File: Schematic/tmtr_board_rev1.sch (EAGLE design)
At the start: 25 parts, among them IC1 MEGA8-AI, J1 POWER_JACKPTH_LOCK

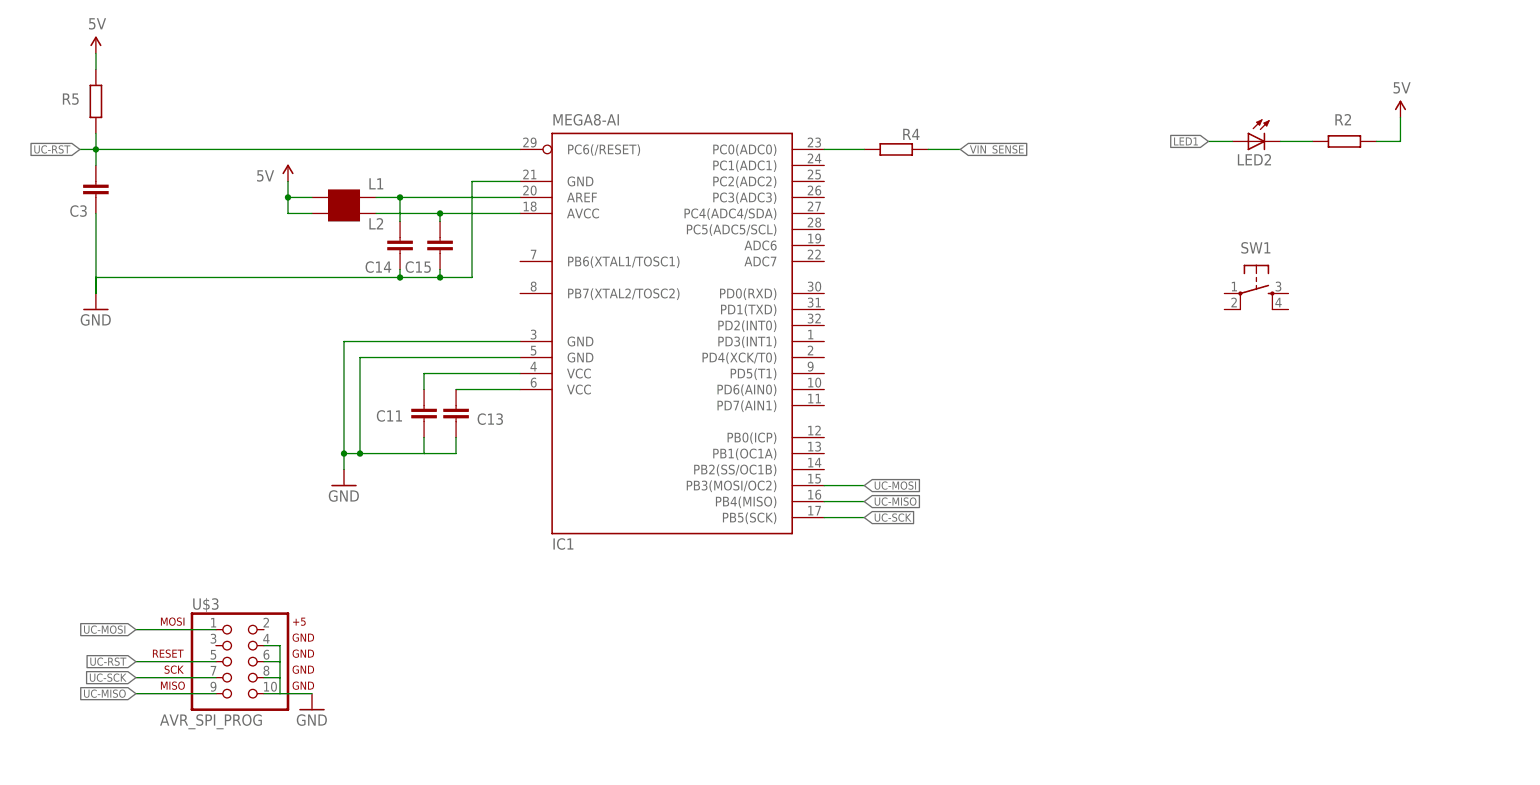
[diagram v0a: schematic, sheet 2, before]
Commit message: 
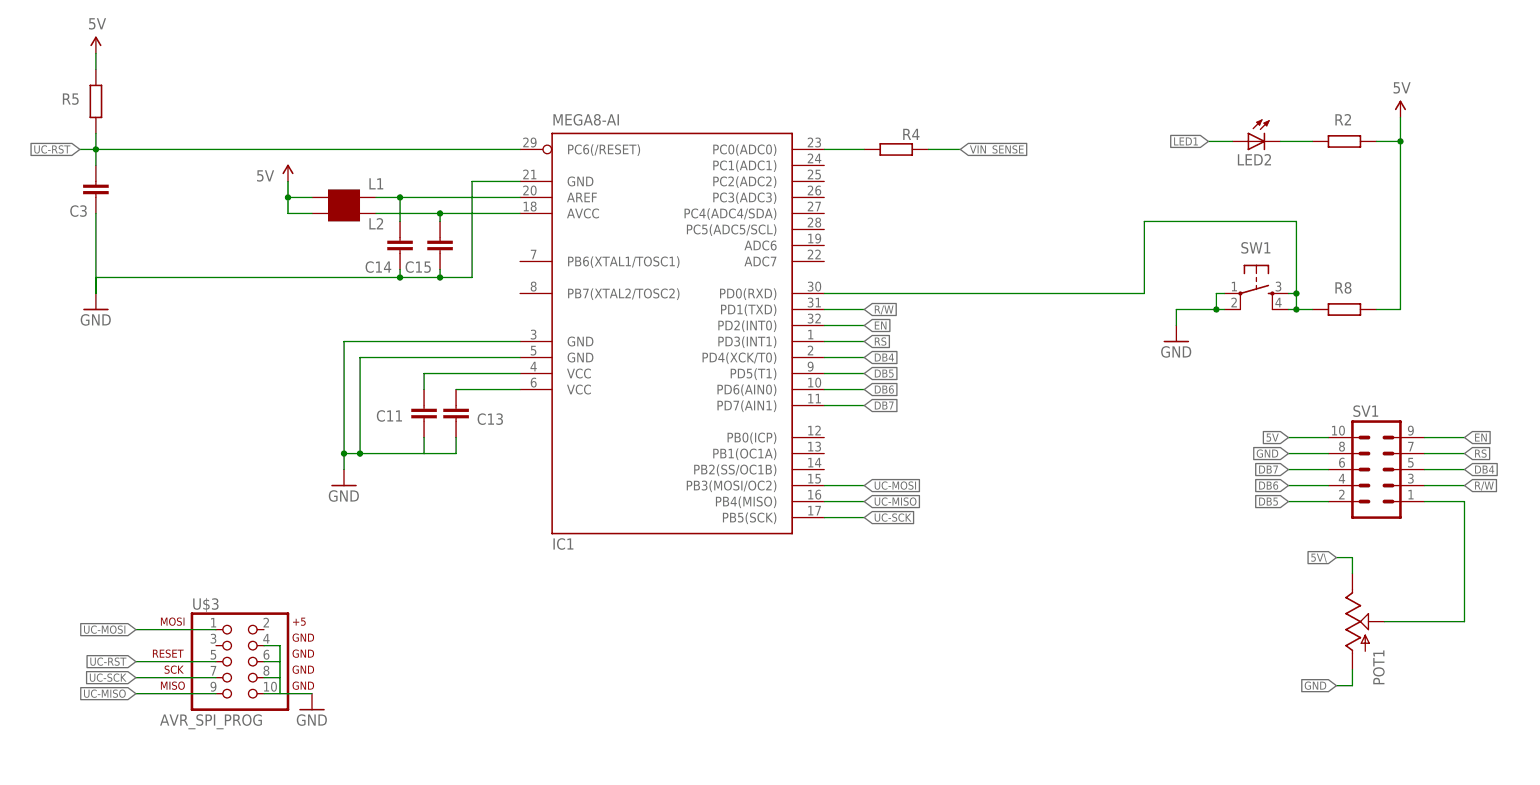
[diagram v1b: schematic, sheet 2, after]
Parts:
- added C12: (no value), rcl:CPOL-EUE2.5-6
- added C6: (no value), SparkFun1:CAPPTH
- added POT1: POT100K_3362U, SparkFun5:POT100K_3362U
- added R6, R7: (no value), resistor:R-EU_0204/5
- added R8: (no value), resistor:R-EU_M0805
- added SV1: (no value), con-lstb:MA05-2
- added U6: V_REG_317SINK, SparkFun4:V_REG_317SINK
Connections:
- new net 3.3V: R7.1, U6.OUT
- new net 5V\: POT1.E
- new net DB4: IC1.PD4(XCK/T0)
- new net DB5: IC1.PD5(T1), SV1.2
- new net DB6: IC1.PD6(AIN0), SV1.4
- new net DB7: IC1.PD7(AIN1), SV1.6
- new net EN: IC1.PD2(INT0)
- new net N$13: POT1.S, SV1.1
- new net N$20: R6.2, R7.2, U6.ADJ
- new net N$21: C12.+, C6.2
- new net N$9: IC1.PD0(RXD), R8.2, SW1.3, SW1.4
- new net R/W: IC1.PD1(TXD)
- new net RS: IC1.PD3(INT1)
- net 5V: now also R8.1, SV1.10, U6.IN
- net GND: now also C12.-, C6.1, POT1.A, R6.1, SV1.8, SW1.1, SW1.2

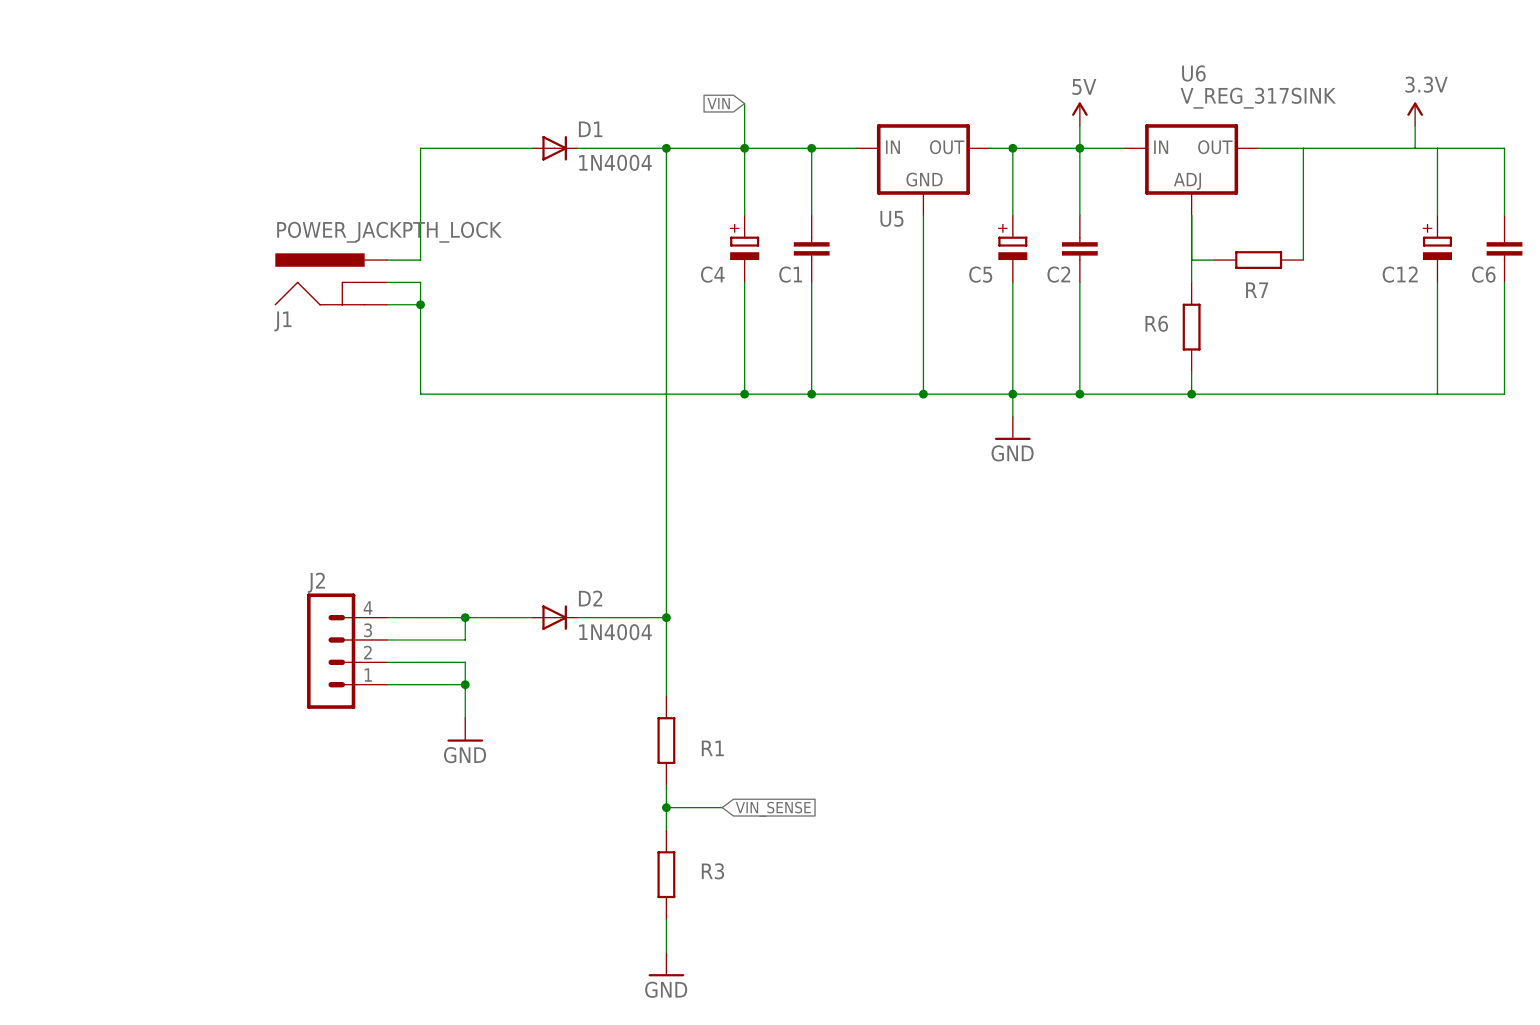
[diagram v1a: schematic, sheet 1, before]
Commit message: 
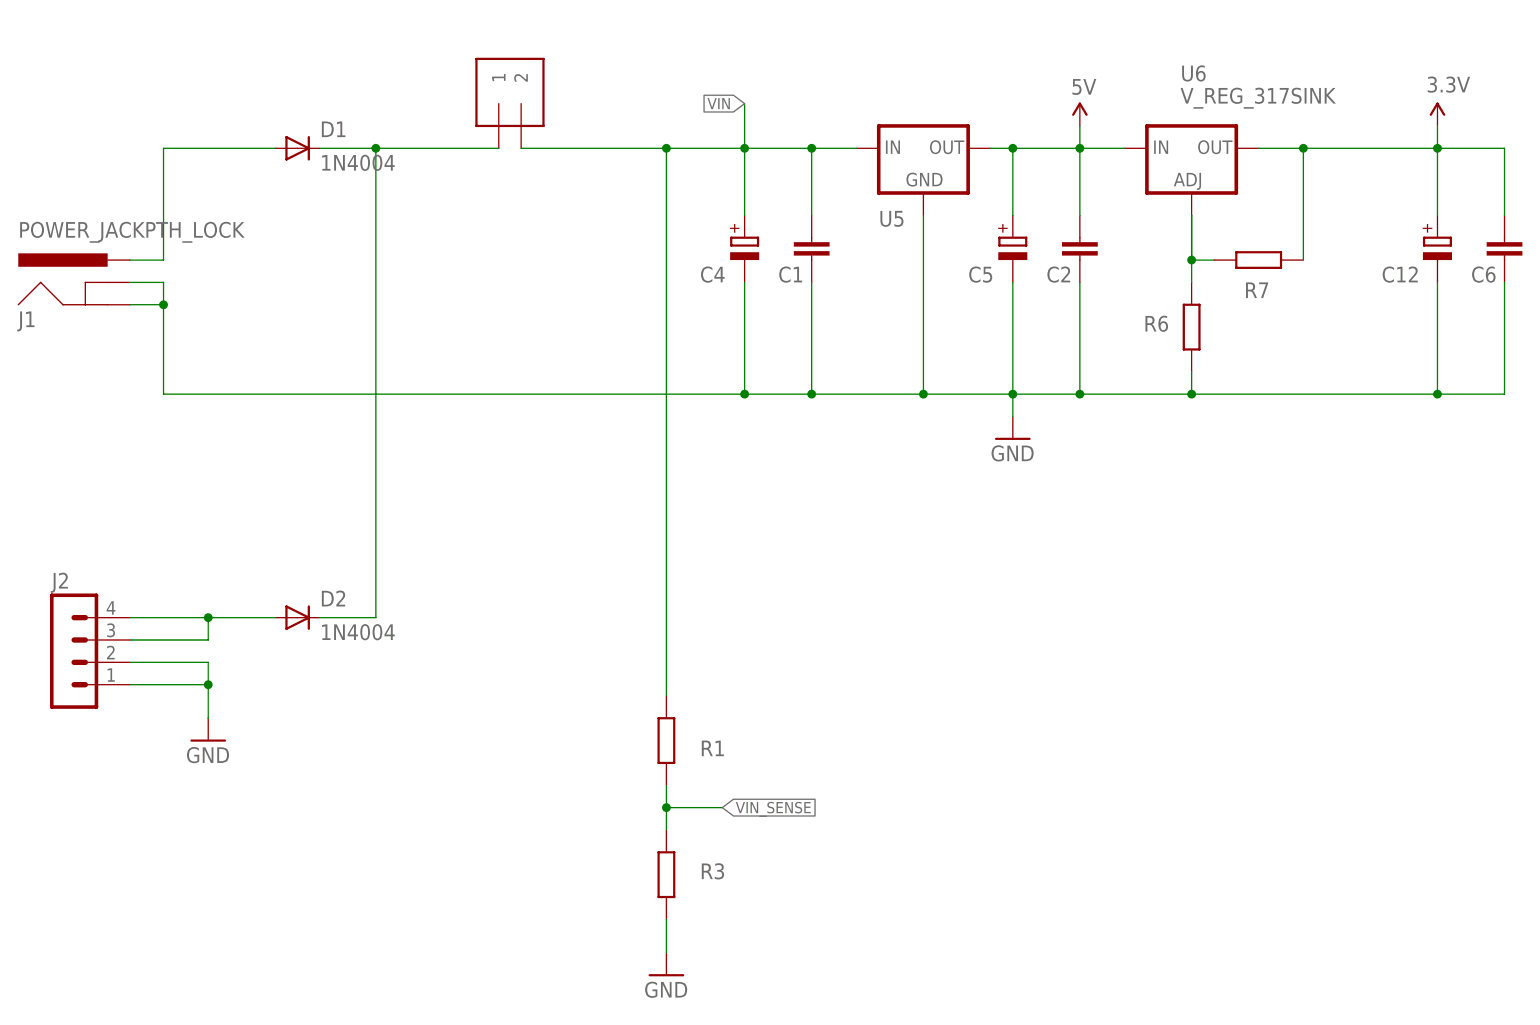
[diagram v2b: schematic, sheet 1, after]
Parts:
- added C7, C8: (no value), SparkFun1:CAP0805
- added IC2, IC3: MAX31855, adafruit:MAX6675
- added J3, J4, J5: 1X2-3.5MM, adafruit:1X2-3.5MM
- added LED1: (no value), led:LEDCHIPLED_0805
- added R9: (no value), resistor:R-EU_M0805
- renumbered SW1 to AVG_SW
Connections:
- removed net 5V\: POT1.E
- removed net N$21: C12.+, C6.2
- removed net N$8: C13.2, IC1.VCC@2
- new net CS_TS_IC0: IC1.PC4(ADC4/SDA), IC2./CS
- new net CS_TS_IC1: IC1.PB1(OC1A), IC3./CS
- new net DO_TS_IC0: IC1.PC3(ADC3), IC2.DO
- new net DO_TS_IC1: IC1.PB0(ICP), IC3.DO
- new net LED2: IC1.PC2(ADC2), LED2.A
- new net N$10: LED1.C, R9.2
- new net SCK_TS_IC0: IC1.PC5(ADC5/SCL), IC2.SCK
- new net SCK_TS_IC1: IC1.PB2(SS/OC1B), IC3.SCK
- new net T+0: IC2.T+, J3.1
- new net T+1: IC3.T+, J4.1
- new net T-0: IC2.T-, J3.2
- new net T-1: IC3.T-, J4.2
- net 3.3V: now also C12.+, C6.2, C7.1, C8.1, IC2.VCC, IC3.VCC
- net 5V: now also C11.2, C13.2, IC1.VCC@1, IC1.VCC@2, POT1.E, R9.1
- net GND: now also C7.2, C8.2, IC2.GND, IC3.GND
- net LED1: now also IC1.PC1(ADC1), LED1.A; no longer LED2.A
- net N$4: now also D1.C, D2.C, J5.1; no longer C11.2, IC1.VCC@1
- net VIN: now also J5.2; no longer D1.C, D2.C
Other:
- moved on the sheet: D1, D2, J1, J2

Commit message: 
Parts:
- removed AVG_SW: (no value), SparkFun1:TAC_SWITCHPTH
- removed C14: (no value), SparkFun1:CAP0805
- removed IC3: MAX31855, adafruit:MAX6675
- removed LED1, LED2: (no value), led:LEDCHIPLED_0805
- removed POT1: POT100K_3362U, SparkFun5:POT100K_3362U
- removed SV1: (no value), con-lstb:MA05-2
- removed U6: V_REG_317SINK, SparkFun4:V_REG_317SINK
- added C10: (no value), SparkFun1:CAP0805
- added J7, J8: 22-23-2021, con-molex:22-23-2021
- added LED3, LED4: (no value), led:LEDCHIPLED_0805
- added R10, R11: (no value), resistor:R-EU_M0805
- added U1: (no value), v-reg:78XXS
- added U2: LD117AS12TR, v-reg:LD117AS12TR
- C1: device SparkFun1:CAPPTH -> rcl:CPOL-EUE5-6
- C12: device rcl:CPOL-EUE2.5-6 -> SparkFun1:CAP0805
- C3: device SparkFun1:CAP0805 -> rcl:CPOL-EUE2.5-6
- C4: device rcl:CPOL-EUE5-6 -> SparkFun1:CAPPTH
- D1, D2: value 1N4004 -> (none); device diode:1N4004 -> semicon-smd-ipc:D-FILL-SMB
- J1: value POWER_JACKPTH_LOCK -> 22-23-2021; device SparkFun4:POWER_JACKPTH_LOCK -> con-molex:22-23-2021
- J2: value (none) -> POWER_JACKPTH_LOCK; device con-lstb:MA04-1 -> SparkFun4:POWER_JACKPTH_LOCK
- J3: value 1X2-3.5MM -> (none); device adafruit:1X2-3.5MM -> con-lstb:MA04-1
- J4: value 1X2-3.5MM -> 22-23-2021; device adafruit:1X2-3.5MM -> con-molex:22-23-2021
- J5: value 1X2-3.5MM -> (none); device adafruit:1X2-3.5MM -> con-lstb:MA05-2
- R6, R7: device resistor:R-EU_0204/5 -> resistor:R-EU_M0805
- U5: value (none) -> MAX31855; device v-reg:78XXS -> adafruit:MAX6675
- renumbered C15 to C9, IC1 to U3, IC2 to U4, U$3 to J6
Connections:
- net 3.3V: now also C12.1, C13.1, C5.+, R1.2, U2.OUT, U5.VCC; no longer C12.+, C7.1, C8.1, IC3.VCC, R7.1, U6.OUT
- net 5V: now also C10.2, C3.+, C4.2, J5.10, R10.1, R6.1, U1.OUT, U2.IN; no longer C13.2, C2.2, C5.+, POT1.E, R2.1, SV1.10, U5.OUT, U6.IN
- net CS_TS_IC1: now also U5./CS; no longer IC3./CS
- net DB4: now also J5.5
- net DB5: now also J5.2; no longer SV1.2
- net DB6: now also J5.4; no longer SV1.4
- net DB7: now also J5.6; no longer SV1.6
- net DO_TS_IC1: now also U5.DO; no longer IC3.DO
- net EN: now also J5.9
- net GND: now also C1.-, C10.1, C12.2, C13.2, C3.-, C4.1, C7.1, J2.GND, J2.GNDBREAK, J3.1, J3.2, J4-2.S, J5.8, R11.2, R2.2, R4.2, U1.GND; no longer AVG_SW.1, AVG_SW.2, C1.1, C12.-, C13.1, C3.1, C4.-, C7.2, C8.2, IC3.GND, J1.GND, J1.GNDBREAK, J2.1, J2.2, POT1.A, R3.2, R6.1, SV1.8
- net LED1: now also LED4.C; no longer LED1.A
- net LED2: now also LED3.C; no longer LED2.A
- net N$1: now also J2.PWR; no longer J1.PWR
- net N$10: now also LED4.A, R8.2; no longer LED1.C, R9.2
- net N$12: now also LED3.A, R6.2; no longer LED2.C, R2.2
- net N$13: now also J5.1, R10.2, R11.1; no longer POT1.S, SV1.1
- net N$2: now also J3.3, J3.4; no longer J2.3, J2.4
- net N$20: now also R1.1, R2.1, U2.ADJ; no longer R6.2, R7.2, U6.ADJ
- net N$3: now also R7.2, U3.ADC6; no longer R4.2, U3.PC0(ADC0)
- net N$4: now also J1-1.S; no longer J5.1
- net N$5: now also C8.2; no longer C14.2
- net N$7: now also C8.1; no longer C14.1
- net N$9: now also J4-1.S, R9.2; no longer AVG_SW.3, AVG_SW.4, R8.2
- net R/W: now also J5.3
- net RS: now also J5.7
- net SCK_TS_IC1: now also U5.SCK; no longer IC3.SCK
- net T+0: now also J7-2.S; no longer J3.1
- net T+1: now also J8-2.S, U5.T+; no longer IC3.T+, J4.1
- net T-0: now also J7-1.S; no longer J3.2
- net T-1: now also J8-1.S, U5.T-; no longer IC3.T-, J4.2
- net UC-RST: now also C7.2; no longer C3.2
- net VIN: now also C1.+, C2.2, J1-2.S, R3.1, U1.IN; no longer C1.2, C4.+, J5.2, R1.1, U5.IN
- net VIN_SENSE: now also R3.2, R7.1; no longer R1.2, R3.1
